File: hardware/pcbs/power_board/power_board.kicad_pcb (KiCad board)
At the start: 2 copper layers, 90 x 140 mm, 154 parts, among them J1 Header_01x04, J10 Molex 254 47053, J11 Molex 254 47053, J12 Molex 254 47053, J13 Molex 254 47053, J14 Header_02x03, J15 PJ-102AH, J16 ScrewTerminal_02, J17 ScrewTerminal_02, J18 ScrewTerminal_02, J19 ScrewTerminal_02, J2 Header_01x04, J20 ScrewTerminal_02, J21 Header_02x04, J22 ScrewTerminal_02, J3 USB3_B_Micro, J4 USB3_A, J5 USB_A, J6 USB_A, J7 USB_A, J8 USB_A, J9 Molex 254 47053, Q1 BSS138, Q2 BSS138, Q3 BSS138, Q4 BSS138, Q5 IRFR5305, U1 VRB1205S-6WR3, U10 EMC2305, U11 TCA9534, U12 LMR38020, U13 LMR38020, U14 TMP1075D, U2 LTV-247, U3 NCP380, U4 VRB1205S-6WR3, U5 NCP380, U6 VRB1205S-6WR3, U7 NCP380, U8 VRB1205S-6WR3, U9 NCP380

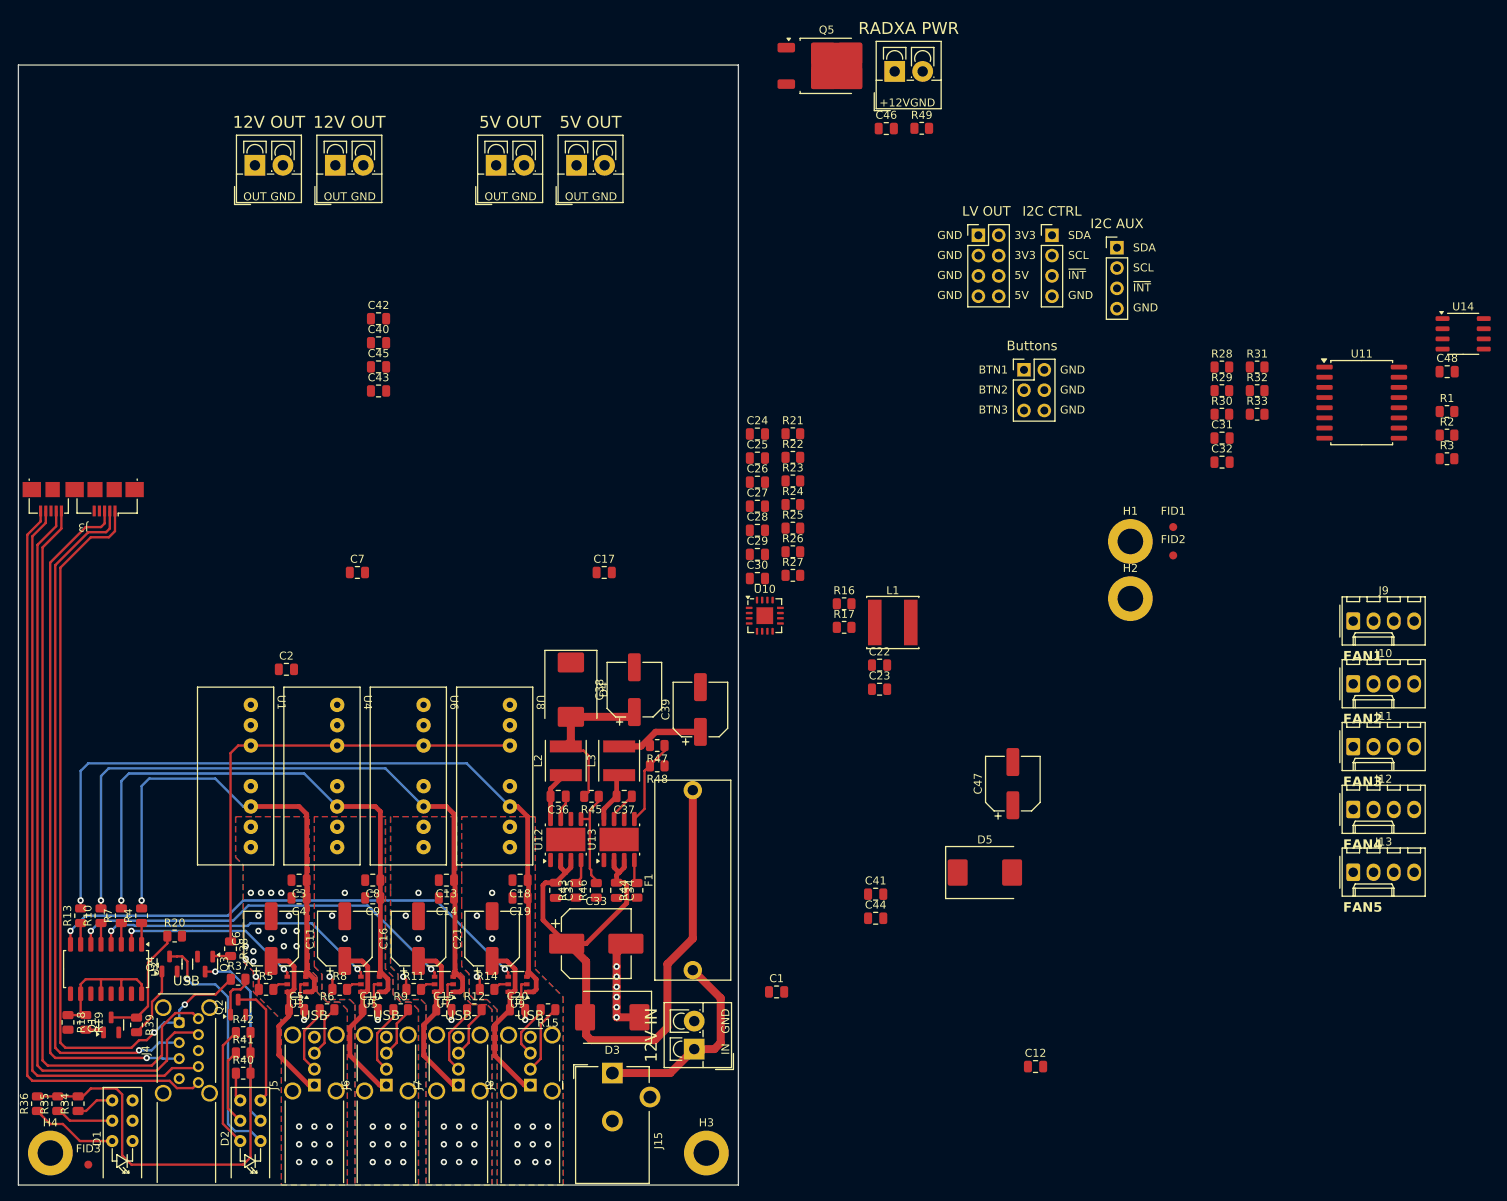
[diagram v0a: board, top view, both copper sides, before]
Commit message: power_board: remove unused caps
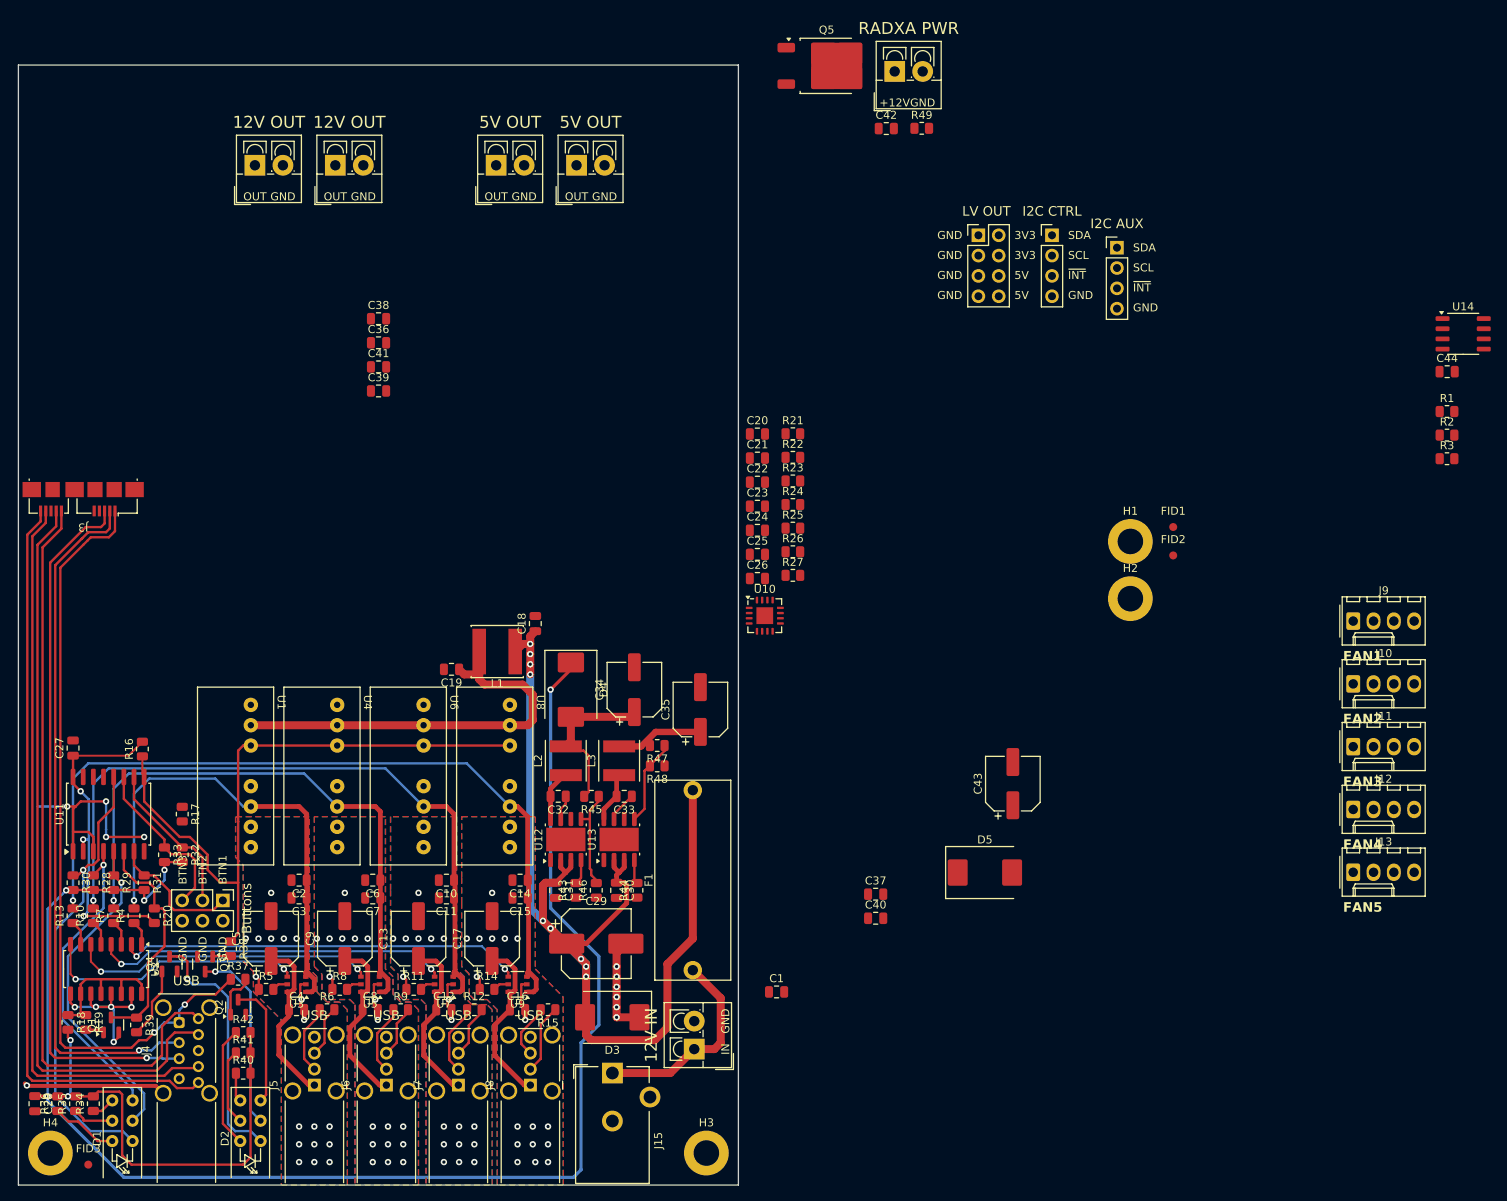
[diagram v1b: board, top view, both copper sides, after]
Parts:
- removed the C12 at (157.1, 159.2)
- removed the C17 at (103.2, 97.4)
- removed the C2 at (63.5, 109.5)
- removed the C7 at (72.4, 97.4)
- moved C28 168.7 mm to (32.1, 163.8), turned to -90 degrees
- moved U11 164.9 mm to (41.3, 127.6), turned to 90 degrees
- moved R28 155.1 mm to (39.4, 136.2), turned to -90 degrees
- moved R30 155.1 mm to (36.8, 136.2), turned to -90 degrees
- moved R31 153.3 mm to (45.7, 136.2), turned to -90 degrees
- moved R29 151.6 mm to (41.9, 136.2), turned to -90 degrees
- moved C27 148.8 mm to (36.8, 119.4), turned to 90 degrees
- moved R33 147.3 mm to (48.3, 132.7), turned to -90 degrees
- moved R32 146.4 mm to (50.5, 132.7), turned to -90 degrees
- moved J14 120.1 mm to (55.6, 138.4), turned to -90 degrees
- moved R16 89.6 mm to (45.5, 119.5), turned to 90 degrees
- moved R17 86.0 mm to (50.5, 127.6), turned to -90 degrees
- moved C19 53.6 mm to (84.1, 109.5), turned to 180 degrees
- moved L1 49.6 mm to (89.9, 107.3), turned to 180 degrees
- moved C18 43.3 mm to (94.6, 103.8), turned to 90 degrees
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- renumbered C13 to C10, C14 to C11, C15 to C12, C16 to C13, C18 to C14, C19 to C15, C20 to C16, C21 to C17, C22 to C18, C23 to C19, C3 to C2, C24 to C20, C25 to C21, C26 to C22, C27 to C23, C28 to C24, C29 to C25, C30 to C26, C31 to C27, C32 to C28, C33 to C29, C4 to C3, C34 to C30, C35 to C31, C36 to C32, C37 to C33, C38 to C34, C39 to C35, C40 to C36, C41 to C37, C42 to C38, C43 to C39, C5 to C4, C44 to C40, C45 to C41, C46 to C42, C47 to C43, C48 to C44, C6 to C5, C8 to C6, C9 to C7, C10 to C8, C11 to C9
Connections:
- net Net-(D1-GK) renamed /GPIOs/LED1
- net Net-(D1-YK) renamed /GPIOs/LED2
- net Net-(J14-Pin_1) renamed /GPIOs/BTN1
- D1 pad 2: Net-(D1-RK) -> /GPIOs/LED3
- J14 pad 3: Net-(J14-Pin_3) -> /GPIOs/BTN2
- J14 pad 5: Net-(J14-Pin_5) -> /GPIOs/BTN3
- R18 pad 2: +3.3V -> +5V
- R30 pad 1: Net-(D1-RK) -> /GPIOs/LED3
- R32 pad 1: Net-(J14-Pin_3) -> /GPIOs/BTN2
- R33 pad 1: Net-(J14-Pin_5) -> /GPIOs/BTN3
- U11 pad 10: Net-(J14-Pin_5) -> /GPIOs/BTN2
- U11 pad 11: /GPIOs/GPIO6 -> /GPIOs/BTN3
- U11 pad 12: /GPIOs/GPIO7 -> /GPIOs/LED3
- U11 pad 6: Net-(D1-RK) -> /GPIOs/GPIO7
- U11 pad 9: Net-(J14-Pin_3) -> /GPIOs/GPIO6
- U2 pad 1: Net-(R4-Pad1) -> Net-(R13-Pad1)
- U2 pad 2: Net-(U3-~{FLAG}) -> Net-(U9-~{FLAG})
- U2 pad 3: Net-(R7-Pad1) -> Net-(R10-Pad1)
- U2 pad 4: Net-(U5-~{FLAG}) -> Net-(U7-~{FLAG})
- U2 pad 5: Net-(R10-Pad1) -> Net-(R7-Pad1)
- U2 pad 6: Net-(U7-~{FLAG}) -> Net-(U5-~{FLAG})
- U2 pad 7: Net-(R13-Pad1) -> Net-(R4-Pad1)
- U2 pad 8: Net-(U9-~{FLAG}) -> Net-(U3-~{FLAG})
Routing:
- net +5V: track 51.4 -> 246.7 mm, vias 0 -> 7
- net GND: track 12.5 -> 81.0 mm, vias 6 -> 16
- net /GPIOs/LED3: track 0.00 -> 56.8 mm, vias 0 -> 1
- net /Isolated chargers/Isolated charger 1/VIN: track 0.00 -> 52.4 mm
- net +12V: track 88.6 -> 137.2 mm, vias 0 -> 9
- net +3.3V: track 10.9 -> 53.3 mm, vias 0 -> 3
- net /GPIOs/LED2: track 0.00 -> 41.4 mm, vias 0 -> 1
- net /GPIOs/LED1: track 0.00 -> 38.7 mm, vias 0 -> 1
- net /GPIOs/GPIO6: track 58.9 -> 81.3 mm
- net /GPIOs/BTN3: track 0.00 -> 21.1 mm
- net /GPIOs/BTN2: track 0.00 -> 19.8 mm
- net /GPIOs/BTN1: track 0.00 -> 16.7 mm
- net /GPIOs/GPIO7: track 15.0 -> 29.0 mm
- net Net-(U9-~{FLAG}): track 62.2 -> 50.6 mm
- net Net-(U3-~{FLAG}): track 23.8 -> 33.1 mm
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
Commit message: power_board: arrange stuff on board
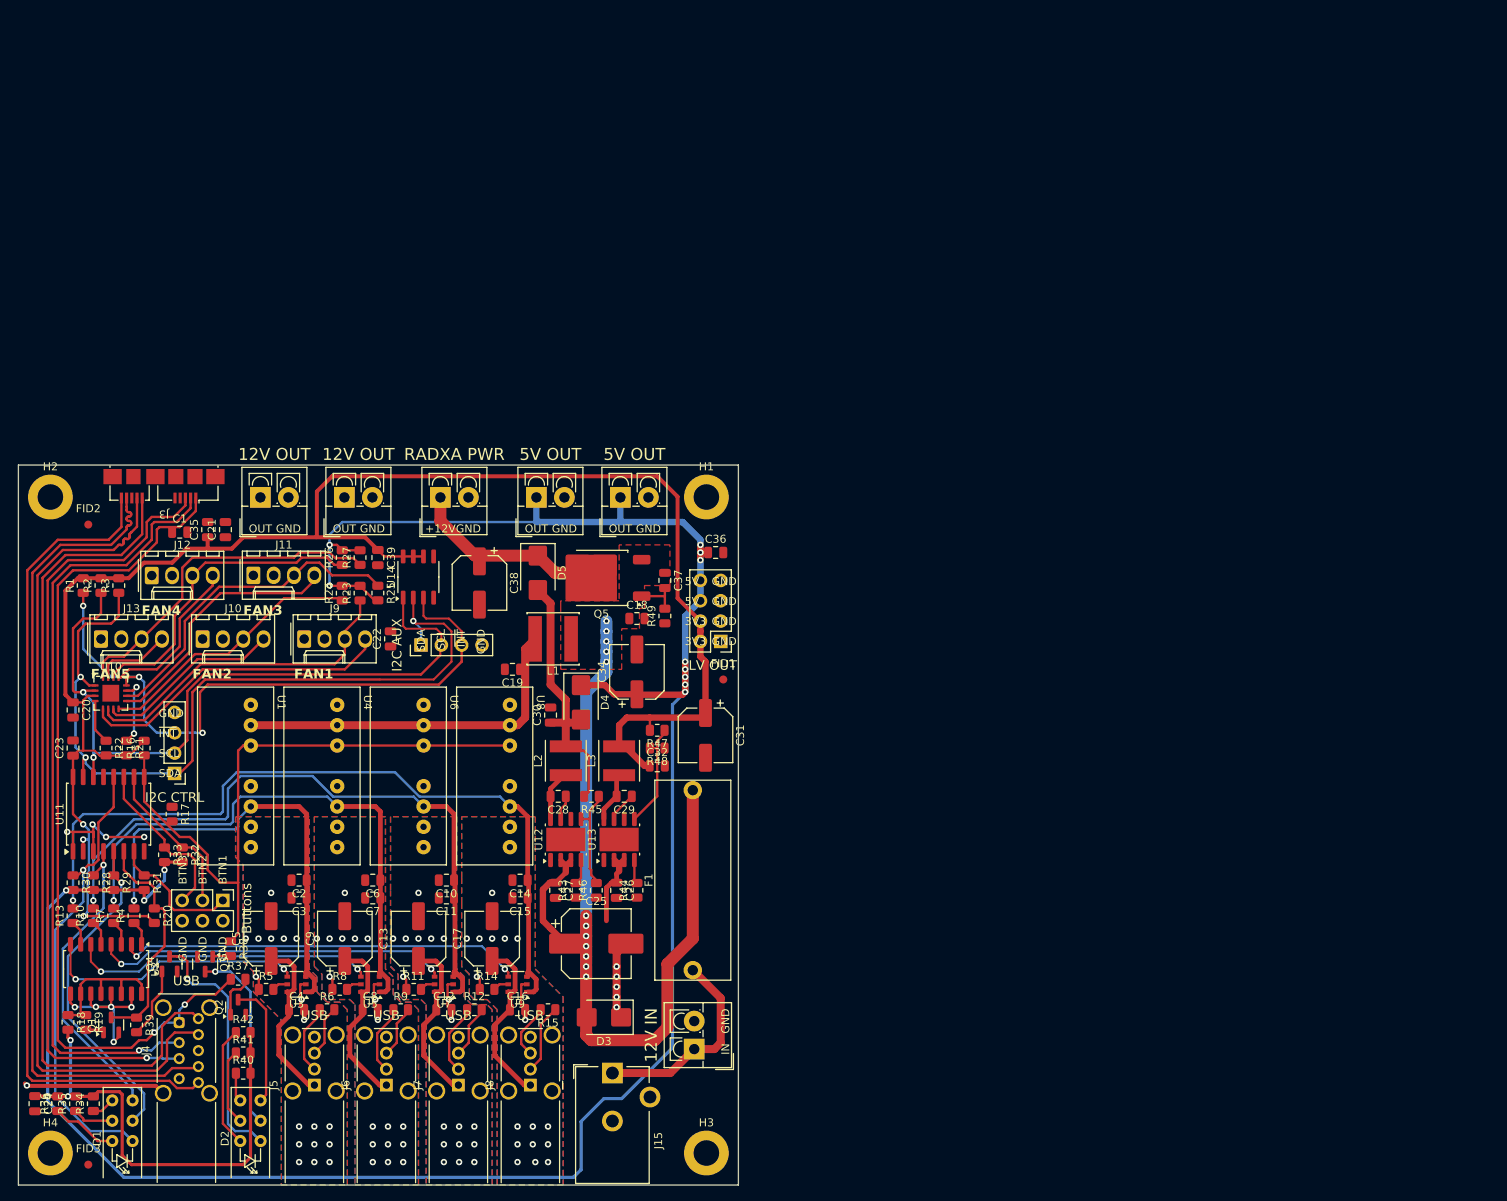
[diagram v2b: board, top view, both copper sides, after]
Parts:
- removed the C23 at (122.4, 89.2)
- removed the C24 at (122.4, 92.2)
- removed the C25 at (122.4, 95.2)
- removed the C26 at (122.4, 98.2)
- removed the C37 at (137.2, 137.6)
- removed the C38 at (75.0, 65.7)
- removed C40: 100nF, Capacitor_SMD:C_0805_2012Metric
- added C30: 10μF, Capacitor_SMD:C_0805_2012Metric, F.Cu at (96.5, 115.3)
- C21: value 100nF -> 10μF
- C22: value 1μF -> 10μF
- D3, D4: value a nice diode -> S2A; footprint Diode_SMD:D_SMC -> Diode_SMD:D_SMB
- D5: footprint Diode_SMD:D_SMC -> Diode_SMD:D_SMB
- moved R1 171.9 mm to (38.1, 99.1), turned to 90 degrees
- moved R2 169.3 mm to (40.3, 99.1), turned to 90 degrees
- moved R3 166.8 mm to (42.5, 99.1), turned to 90 degrees
- moved J13 159.2 mm to (40.3, 105.7)
- moved J12 153.0 mm to (46.7, 97.8)
- moved J10 143.9 mm to (53.0, 105.7)
- moved J11 139.1 mm to (59.4, 97.8)
- moved FID2 135.7 mm to (38.7, 91.4)
- moved C39 135.7 mm to (74.9, 95.6), turned to -90 degrees
- moved H2 135.6 mm to (34.0, 88.0)
- moved U14 134.1 mm to (80.0, 98.0), turned to 90 degrees
- moved J9 131.1 mm to (65.7, 105.7)
- moved J1 128.7 mm to (49.5, 122.5), turned to 180 degrees
- moved J2 100.2 mm to (80.3, 106.5), turned to 90 degrees
- moved C1 94.2 mm to (50.2, 92.4)
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- renumbered C27 to C23, C28 to C24, C29 to C25, C30 to C26, C31 to C27, C32 to C28, C33 to C29, C35 to C31, C36 to C32, C39 to C35, C41 to C36, C42 to C37, C43 to C38, C44 to C39
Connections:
- C21 pad 1: +3.3V -> +12V
- C34 pad 1: +6V -> +5V
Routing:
- net +3.3V: track 53.3 -> 218.3 mm
- net +5V: track 246.7 -> 357.2 mm, vias 7 -> 16
- net /Fan Controller/SDA: track 0.00 -> 103.5 mm, vias 0 -> 3
- net /Fan Controller/SCL: track 0.00 -> 92.1 mm, vias 0 -> 2
- net /Fan Controller/~{ALERT}: track 0.00 -> 82.7 mm, vias 0 -> 3
- net Net-(J13-Pin_3): track 0.00 -> 42.6 mm
- net Net-(J11-Pin_3): track 0.00 -> 41.6 mm
- net Net-(J9-Pin_3): track 0.00 -> 41.5 mm
- net Net-(J9-Pin_4): track 0.00 -> 39.4 mm
- net Net-(J12-Pin_3): track 0.00 -> 39.2 mm
- net Net-(J10-Pin_3): track 0.00 -> 33.8 mm
- net Net-(J11-Pin_4): track 0.00 -> 32.4 mm
- net Net-(J10-Pin_4): track 0.00 -> 23.3 mm
- net Net-(D5-K): track 0.00 -> 22.6 mm
- net Net-(J12-Pin_4): track 0.00 -> 19.8 mm
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- added copper zone on F.Cu, net +12V
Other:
- board size 90 x 140 mm -> 90 x 90 mm

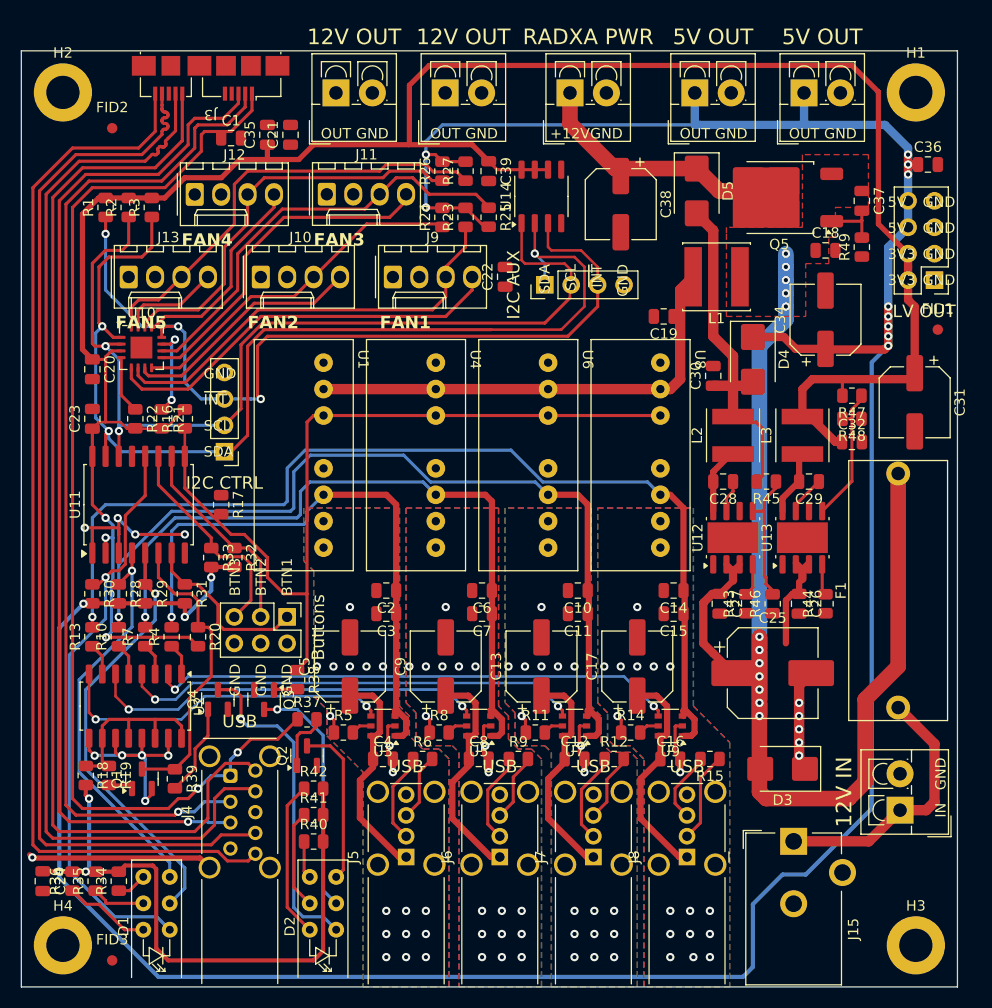
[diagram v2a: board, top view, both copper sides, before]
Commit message: power_board: fix drc errors
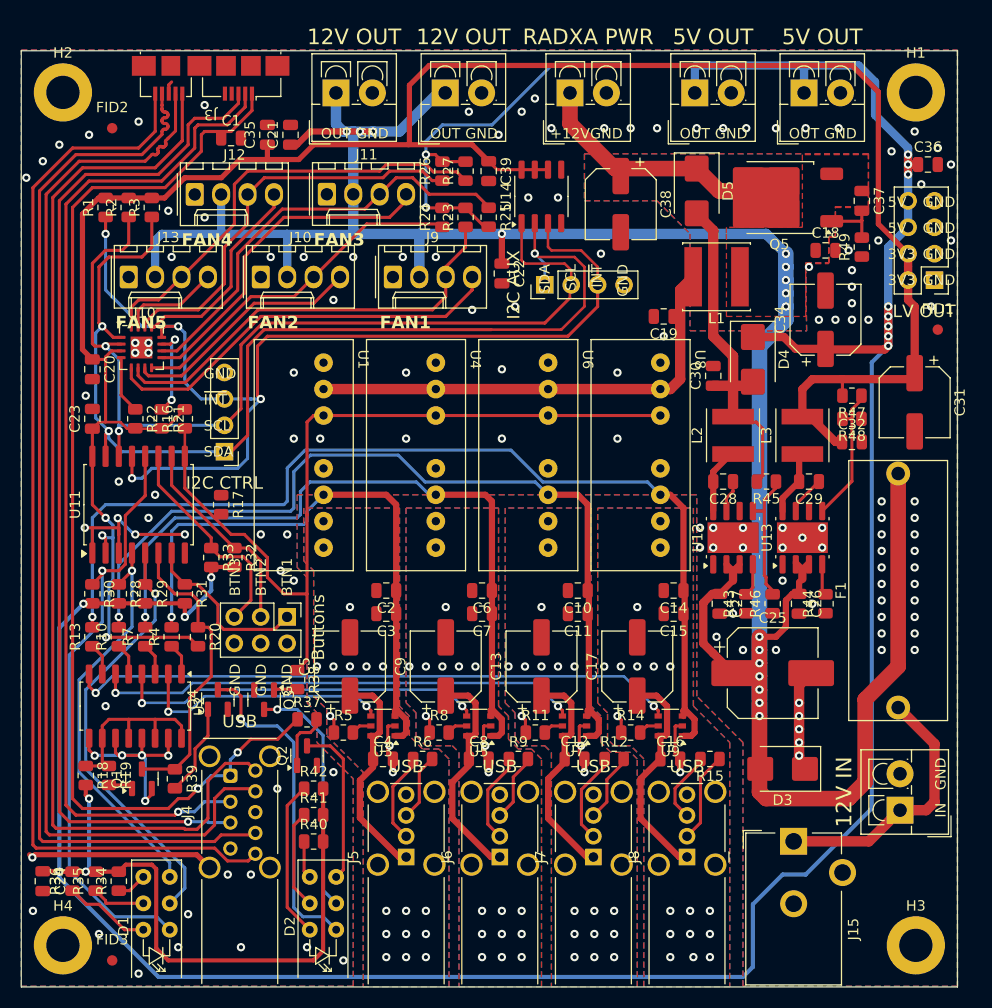
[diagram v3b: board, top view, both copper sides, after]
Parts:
- moved C22 0.45 mm to (76.2, 105.4), turned to -90 degrees
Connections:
- U2 pad 1: Net-(R13-Pad1) -> Net-(R4-Pad1)
- U2 pad 2: Net-(U9-~{FLAG}) -> Net-(U3-~{FLAG})
- U2 pad 3: Net-(R10-Pad1) -> Net-(R7-Pad1)
- U2 pad 4: Net-(U7-~{FLAG}) -> Net-(U5-~{FLAG})
- U2 pad 5: Net-(R7-Pad1) -> Net-(R10-Pad1)
- U2 pad 6: Net-(U5-~{FLAG}) -> Net-(U7-~{FLAG})
- U2 pad 7: Net-(R4-Pad1) -> Net-(R13-Pad1)
- U2 pad 8: Net-(U3-~{FLAG}) -> Net-(U9-~{FLAG})
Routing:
- net +12V: track 126.7 -> 241.8 mm, vias 12 -> 16
- net /Fan Controller/~{ALERT}: track 82.7 -> 102.9 mm, vias 3 -> 4
- net Net-(U3-~{FLAG}): track 33.1 -> 24.8 mm
- net Net-(U9-~{FLAG}): track 50.6 -> 58.7 mm
- net +5V: track 357.2 -> 362.5 mm
- net Net-(U5-~{FLAG}): track 38.6 -> 35.9 mm
- net Net-(U7-~{FLAG}): track 44.4 -> 46.8 mm
- net GND: track 67.5 -> 69.0 mm, vias 15 -> 138
- net +3.3V: track 218.3 -> 219.1 mm
- net /GPIOs/LED3: track 56.8 -> 57.5 mm
- added copper zone on B.Cu, net GND
- added copper zone on F.Cu, net GND

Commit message: power_board: finalise silkscreen
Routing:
- net +12V: track 241.8 -> 240.3 mm, vias 16 -> 14
